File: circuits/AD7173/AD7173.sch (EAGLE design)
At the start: 35 parts, among them IC1 AD7173, IC2 ADP1720, IC3 ADP1720ARMZ-5, IC4 ADR445BR, Q1 FA-20H

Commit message: upadted AD7173 breakout board
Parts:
- added C16: 4.7uF, rcl:C-EUC0402
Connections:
- net GND: now also C16.2
- net N$28: now also C16.1
- net N$30: now also C15.1
- net VIN: no longer C15.1
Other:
- moved on the sheet: C15, L1
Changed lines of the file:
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@@
 <part name="LED2" library="led" deviceset="LED" device="CHIP-LED0603"/>
 <part name="R5" library="rcl" deviceset="R-EU_" device="R0402" value="220"/>
+<part name="C16" library="rcl" deviceset="C-EU" device="C0402" value="4.7uF"/>
 </parts>
 <sheets>
@@
 <instance part="P+2" gate="VCC" x="127" y="96.52"/>
 <instance part="P+1" gate="VCC" x="162.56" y="35.56"/>
-<instance part="L1" gate="G$1" x="241.3" y="43.18"/>
-<instance part="C15" gate="G$1" x="231.14" y="38.1"/>
+<instance part="L1" gate="G$1" x="233.68" y="43.18"/>
+<instance part="C15" gate="G$1" x="243.84" y="30.48"/>
 <instance part="P+4" gate="1" x="12.7" y="99.06"/>
 <instance part="SJ1" gate="1" x="246.38" y="63.5" rot="R270"/>
@@
 <instance part="LED2" gate="G$1" x="182.88" y="40.64" rot="R270"/>
 <instance part="R5" gate="G$1" x="198.12" y="40.64"/>
+<instance part="C16" gate="G$1" x="254" y="30.48"/>
 </instances>
 <busses>
@@
 <pinref part="POWER" gate="A" pin="3"/>
 <pinref part="GND5" gate="1" pin="GND"/>
-<wire x1="226.06" y1="12.7" x2="231.14" y2="12.7" width="0.1524" layer="91"/>
-<wire x1="231.14" y1="12.7" x2="231.14" y2="30.48" width="0.1524" layer="91"/>
+<wire x1="226.06" y1="12.7" x2="243.84" y2="12.7" width="0.1524" layer="91"/>
 <pinref part="IC4" gate="G$1" pin="GND"/>
 <pinref part="C11" gate="G$1" pin="2"/>
@@
 <wire x1="162.56" y1="12.7" x2="172.72" y2="12.7" width="0.1524" layer="91"/>
 <wire x1="172.72" y1="12.7" x2="172.72" y2="15.24" width="0.1524" layer="91"/>
-<junction x="231.14" y="30.48"/>
-<wire x1="264.16" y1="38.1" x2="259.08" y2="38.1" width="0.1524" layer="91"/>
-<wire x1="259.08" y1="38.1" x2="259.08" y2="30.48" width="0.1524" layer="91"/>
+<junction x="243.84" y="12.7"/>
 <pinref part="C15" gate="G$1" pin="2"/>
-<wire x1="259.08" y1="30.48" x2="231.14" y2="30.48" width="0.1524" layer="91"/>
-<wire x1="231.14" y1="30.48" x2="231.14" y2="33.02" width="0.1524" layer="91"/>
+<wire x1="254" y1="12.7" x2="243.84" y2="12.7" width="0.1524" layer="91"/>
+<wire x1="243.84" y1="12.7" x2="243.84" y2="25.4" width="0.1524" layer="91"/>
 <junction x="172.72" y="12.7"/>
 <pinref part="LED2" gate="G$1" pin="C"/>
@@
 <wire x1="226.06" y1="12.7" x2="226.06" y2="10.16" width="0.1524" layer="91"/>
 <junction x="162.56" y="12.7"/>
+<pinref part="C16" gate="G$1" pin="2"/>
+<wire x1="254" y1="25.4" x2="254" y2="12.7" width="0.1524" layer="91"/>
+<wire x1="254" y1="12.7" x2="261.62" y2="12.7" width="0.1524" layer="91"/>
+<wire x1="261.62" y1="12.7" x2="261.62" y2="38.1" width="0.1524" layer="91"/>
+<wire x1="261.62" y1="38.1" x2="264.16" y2="38.1" width="0.1524" layer="91"/>
 </segment>
 <segment>
@@
 <junction x="215.9" y="25.4"/>
 <pinref part="L1" gate="G$1" pin="1"/>
-<wire x1="231.14" y1="43.18" x2="226.06" y2="43.18" width="0.1524" layer="91"/>
 <wire x1="226.06" y1="25.4" x2="226.06" y2="22.86" width="0.1524" layer="91"/>
-<pinref part="C15" gate="G$1" pin="1"/>
-<wire x1="236.22" y1="43.18" x2="231.14" y2="43.18" width="0.1524" layer="91"/>
-<wire x1="231.14" y1="43.18" x2="231.14" y2="40.64" width="0.1524" layer="91"/>
+<wire x1="228.6" y1="43.18" x2="226.06" y2="43.18" width="0.1524" layer="91"/>
 <junction x="226.06" y="43.18"/>
-<junction x="231.14" y="43.18"/>
 </segment>
 </net>
@@
 <pinref part="POWER" gate="A" pin="1"/>
 <pinref part="L1" gate="G$1" pin="2"/>
-<wire x1="264.16" y1="43.18" x2="259.08" y2="43.18" width="0.1524" layer="91"/>
-<wire x1="259.08" y1="43.18" x2="246.38" y2="43.18" width="0.1524" layer="91"/>
+<wire x1="259.08" y1="43.18" x2="251.46" y2="43.18" width="0.1524" layer="91"/>
+<wire x1="251.46" y1="43.18" x2="238.76" y2="43.18" width="0.1524" layer="91"/>
 <wire x1="259.08" y1="43.18" x2="259.08" y2="48.26" width="0.1524" layer="91"/>
 <wire x1="259.08" y1="48.26" x2="220.98" y2="48.26" width="0.1524" layer="91"/>
@@
 <wire x1="220.98" y1="40.64" x2="203.2" y2="40.64" width="0.1524" layer="91"/>
 <junction x="259.08" y="43.18"/>
+<pinref part="C15" gate="G$1" pin="1"/>
+<wire x1="243.84" y1="33.02" x2="243.84" y2="35.56" width="0.1524" layer="91"/>
+<wire x1="243.84" y1="35.56" x2="251.46" y2="35.56" width="0.1524" layer="91"/>
+<wire x1="251.46" y1="35.56" x2="251.46" y2="43.18" width="0.1524" layer="91"/>
+<wire x1="259.08" y1="43.18" x2="264.16" y2="43.18" width="0.1524" layer="91"/>
+<junction x="251.46" y="43.18"/>
 </segment>
 </net>
@@
 <junction x="261.62" y="50.8"/>
 <junction x="254" y="50.8"/>
-</segment>
-</net>
+<pinref part="C16" gate="G$1" pin="1"/>
+<wire x1="264.16" y1="40.64" x2="261.62" y2="40.64" width="0.1524" layer="91"/>
+<wire x1="261.62" y1="40.64" x2="254" y2="40.64" width="0.1524" layer="91"/>
+<wire x1="254" y1="40.64" x2="254" y2="33.02" width="0.1524" layer="91"/>
+<junction x="261.62" y="40.64"/>
+</segment>
+</net>

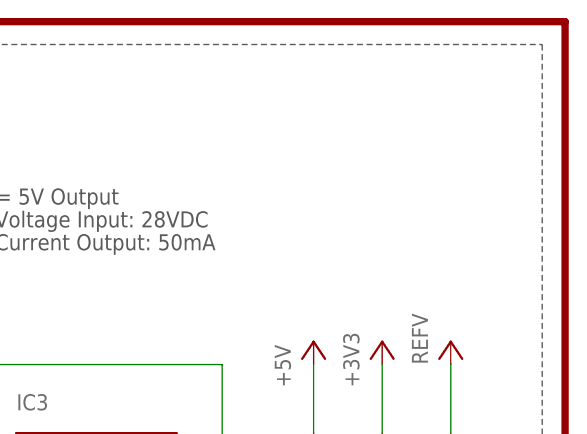
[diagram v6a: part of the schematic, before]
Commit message: updated AD7173 breakout board
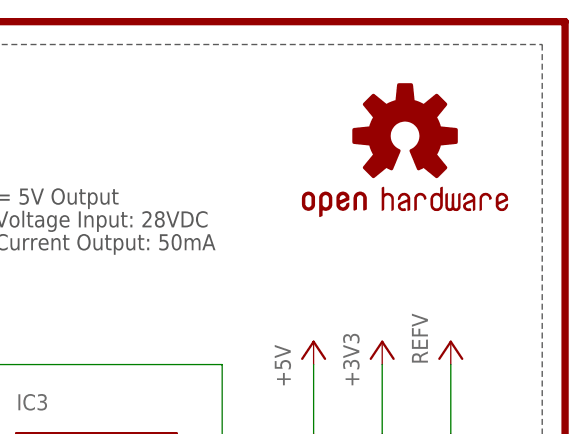
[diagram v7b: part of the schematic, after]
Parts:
- added LOGO1: OSHW-LOGOS, SparkFun-Aesthetics:OSHW-LOGOS
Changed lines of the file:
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@@
 <layer number="54" name="bGND_GNDA" color="7" fill="1" visible="no" active="no"/>
 <layer number="56" name="wert" color="7" fill="1" visible="no" active="no"/>
+<layer number="57" name="tCAD" color="7" fill="1" visible="no" active="no"/>
+<layer number="59" name="tCarbon" color="7" fill="1" visible="no" active="no"/>
+<layer number="60" name="bCarbon" color="7" fill="1" visible="no" active="no"/>
+<layer number="90" name="Modules" color="5" fill="1" visible="yes" active="yes"/>
 <layer number="91" name="Nets" color="2" fill="1" visible="yes" active="yes"/>
 <layer number="92" name="Busses" color="1" fill="1" visible="yes" active="yes"/>
@@
 <layer number="97" name="Info" color="7" fill="1" visible="yes" active="yes"/>
 <layer number="98" name="Guide" color="6" fill="1" visible="yes" active="yes"/>
+<layer number="99" name="SpiceOrder" color="7" fill="1" visible="no" active="no"/>
 <layer number="100" name="Muster" color="7" fill="1" visible="yes" active="yes"/>
 <layer number="101" name="Patch_Top" color="7" fill="1" visible="yes" active="yes"/>
@@
 <layer number="110" name="fp0" color="7" fill="1" visible="yes" active="yes"/>
 <layer number="111" name="border" color="7" fill="1" visible="yes" active="yes"/>
+<layer number="112" name="tSilk" color="7" fill="1" visible="yes" active="yes"/>
+<layer number="113" name="IDFDebug" color="4" fill="1" visible="yes" active="yes"/>
 <layer number="116" name="Patch_BOT" color="7" fill="1" visible="yes" active="yes"/>
 <layer number="121" name="_tsilk" color="7" fill="1" visible="yes" active="yes"/>
@@
 <layer number="124" name="bTestmark" color="7" fill="1" visible="yes" active="yes"/>
 <layer number="125" name="_tNames" color="7" fill="1" visible="yes" active="yes"/>
+<layer number="126" name="_bNames" color="7" fill="1" visible="yes" active="yes"/>
+<layer number="127" name="_tValues" color="7" fill="1" visible="yes" active="yes"/>
+<layer number="128" name="_bValues" color="7" fill="1" visible="yes" active="yes"/>
+<layer number="129" name="Mask" color="7" fill="1" visible="yes" active="yes"/>
 <layer number="131" name="tAdjust" color="7" fill="1" visible="yes" active="yes"/>
 <layer number="132" name="bAdjust" color="7" fill="1" visible="yes" active="yes"/>
 <layer number="144" name="Drill_legend" color="7" fill="1" visible="yes" active="yes"/>
+<layer number="150" name="Notes" color="7" fill="1" visible="yes" active="yes"/>
 <layer number="151" name="HeatSink" color="7" fill="1" visible="yes" active="yes"/>
+<layer number="152" name="_bDocu" color="7" fill="1" visible="yes" active="yes"/>
+<layer number="153" name="FabDoc1" color="7" fill="1" visible="yes" active="yes"/>
+<layer number="154" name="FabDoc2" color="7" fill="1" visible="yes" active="yes"/>
+<layer number="155" name="FabDoc3" color="7" fill="1" visible="yes" active="yes"/>
 <layer number="199" name="Contour" color="7" fill="1" visible="yes" active="yes"/>
 <layer number="200" name="200bmp" color="7" fill="1" visible="yes" active="yes"/>
@@
 <layer number="215" name="215bmp" color="7" fill="1" visible="yes" active="yes"/>
 <layer number="216" name="216bmp" color="7" fill="1" visible="yes" active="yes"/>
+<layer number="217" name="217bmp" color="18" fill="1" visible="no" active="no"/>
+<layer number="218" name="218bmp" color="19" fill="1" visible="no" active="no"/>
+<layer number="219" name="219bmp" color="20" fill="1" visible="no" active="no"/>
+<layer number="220" name="220bmp" color="21" fill="1" visible="no" active="no"/>
+<layer number="221" name="221bmp" color="22" fill="1" visible="no" active="no"/>
+<layer number="222" name="222bmp" color="23" fill="1" visible="no" active="no"/>
+<layer number="223" name="223bmp" color="24" fill="1" visible="no" active="no"/>
+<layer number="224" name="224bmp" color="25" fill="1" visible="no" active="no"/>
+<layer number="225" name="225bmp" color="7" fill="1" visible="yes" active="yes"/>
+<layer number="226" name="226bmp" color="7" fill="1" visible="yes" active="yes"/>
+<layer number="227" name="227bmp" color="7" fill="1" visible="yes" active="yes"/>
+<layer number="228" name="228bmp" color="7" fill="1" visible="yes" active="yes"/>
+<layer number="229" name="229bmp" color="7" fill="1" visible="yes" active="yes"/>
+<layer number="230" name="230bmp" color="7" fill="1" visible="yes" active="yes"/>
+<layer number="231" name="231bmp" color="7" fill="1" visible="yes" active="yes"/>
+<layer number="248" name="Housing" color="7" fill="1" visible="yes" active="yes"/>
+<layer number="249" name="Edge" color="7" fill="1" visible="yes" active="yes"/>
 <layer number="250" name="Descript" color="7" fill="1" visible="yes" active="yes"/>
 <layer number="251" name="SMDround" color="7" fill="1" visible="yes" active="yes"/>
 <layer number="254" name="cooling" color="7" fill="1" visible="yes" active="yes"/>
+<layer number="255" name="routoute" color="7" fill="1" visible="yes" active="yes"/>
 </layers>
 <schematic xreflabel="%F%N/%S.%C%R" xrefpart="/%S.%C%R">
@@
 <part name="R5" library="rcl" deviceset="R-EU_" device="R0402" value="220"/>
 <part name="C16" library="rcl" deviceset="C-EU" device="C0402" value="4.7uF"/>
+<part name="LOGO1" library="SparkFun-Aesthetics" deviceset="OSHW-LOGO" device="S"/>
 </parts>
 <sheets>
@@
 <instance part="R5" gate="G$1" x="198.12" y="40.64"/>
 <instance part="C16" gate="G$1" x="254" y="30.48"/>
+<instance part="LOGO1" gate="G$1" x="256.54" y="101.6"/>
 </instances>
 <busses>

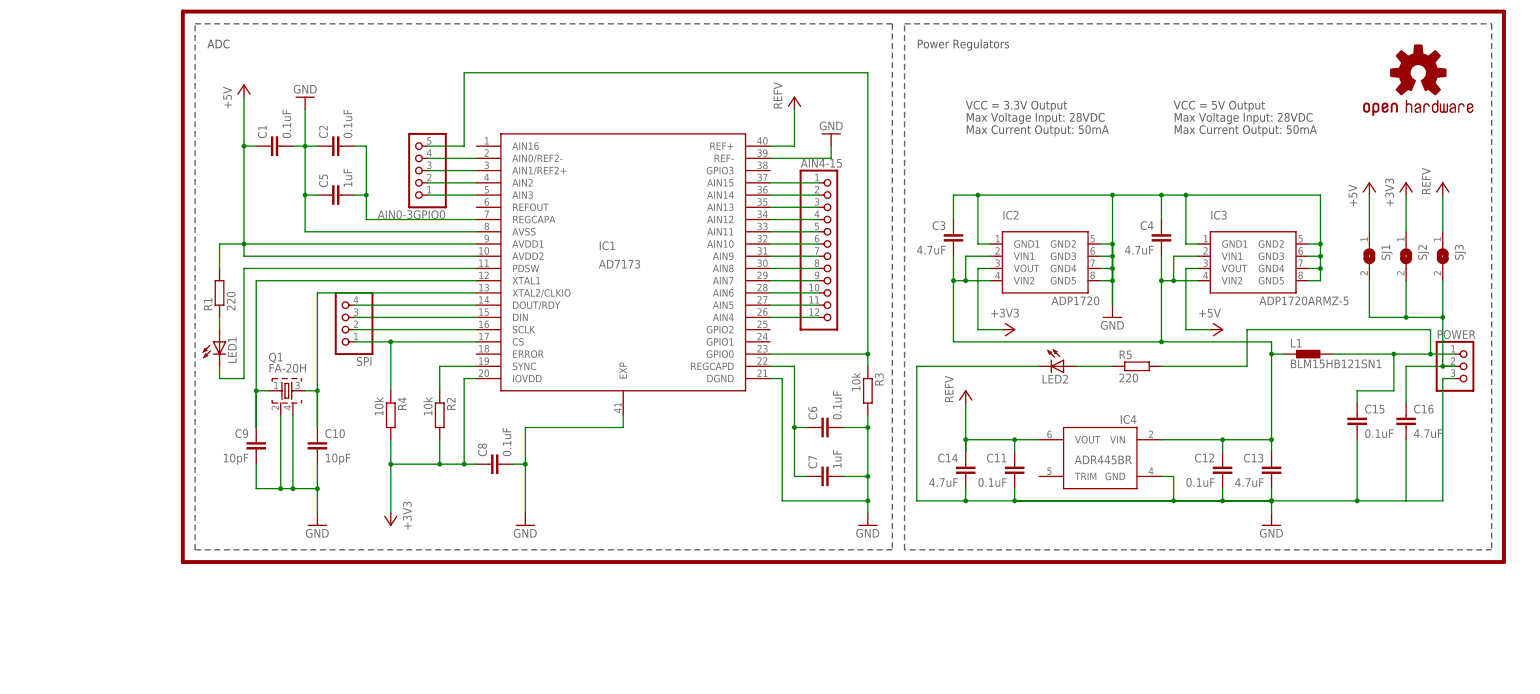
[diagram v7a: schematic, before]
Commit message: updated pins, components placing
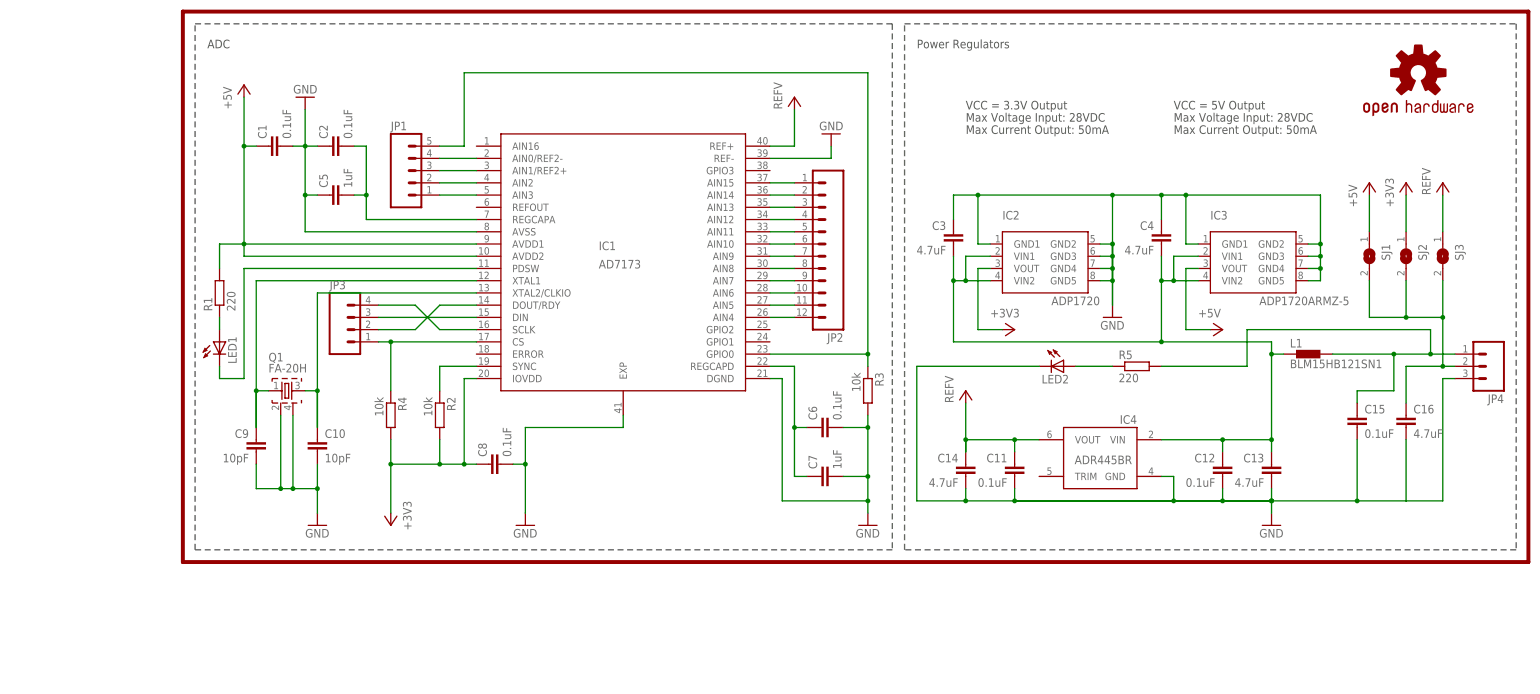
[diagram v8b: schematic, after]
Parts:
- removed AIN0-3GPIO0: (no value), pinhead:PINHD-1X5
- removed AIN4-15: (no value), pinhead:PINHD-1X12
- removed POWER: (no value), pinhead:PINHD-1X3
- removed SPI: (no value), pinhead:PINHD-1X4
- added JP1: (no value), SparkFun-Connectors:M05PTH
- added JP2: (no value), SparkFun-Connectors:M12PTH
- added JP3: (no value), SparkFun-Connectors:M04PTH
- added JP4: (no value), SparkFun-Connectors:M03PTH
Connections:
- net GND: now also JP4.3; no longer POWER.3
- net N$10: now also JP2.5; no longer AIN4-15.5
- net N$11: now also JP2.6; no longer AIN4-15.6
- net N$12: now also JP2.7; no longer AIN4-15.7
- net N$13: now also JP2.8; no longer AIN4-15.8
- net N$14: now also JP2.9; no longer AIN4-15.9
- net N$15: now also JP2.10; no longer AIN4-15.10
- net N$16: now also JP2.11; no longer AIN4-15.11
- net N$17: now also JP2.12; no longer AIN4-15.12
- net N$18: now also JP1.1; no longer AIN0-3GPIO0.1
- net N$19: now also JP1.2; no longer AIN0-3GPIO0.2
- net N$20: now also JP1.3; no longer AIN0-3GPIO0.3
- net N$21: now also JP1.4; no longer AIN0-3GPIO0.4
- net N$23: now also JP3.2; no longer SPI.4
- net N$24: now also JP3.3; no longer SPI.3
- net N$25: now also JP3.4; no longer SPI.2
- net N$28: now also JP4.2; no longer POWER.2
- net N$3: now also JP3.1; no longer SPI.1
- net N$30: now also JP4.1; no longer POWER.1
- net N$4: now also JP2.1; no longer AIN4-15.1
- net N$5: now also JP1.5; no longer AIN0-3GPIO0.5
- net N$7: now also JP2.2; no longer AIN4-15.2
- net N$8: now also JP2.3; no longer AIN4-15.3
- net N$9: now also JP2.4; no longer AIN4-15.4
